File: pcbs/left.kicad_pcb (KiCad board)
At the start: 2 copper layers, 121.1 x 91.2 mm, 27 parts

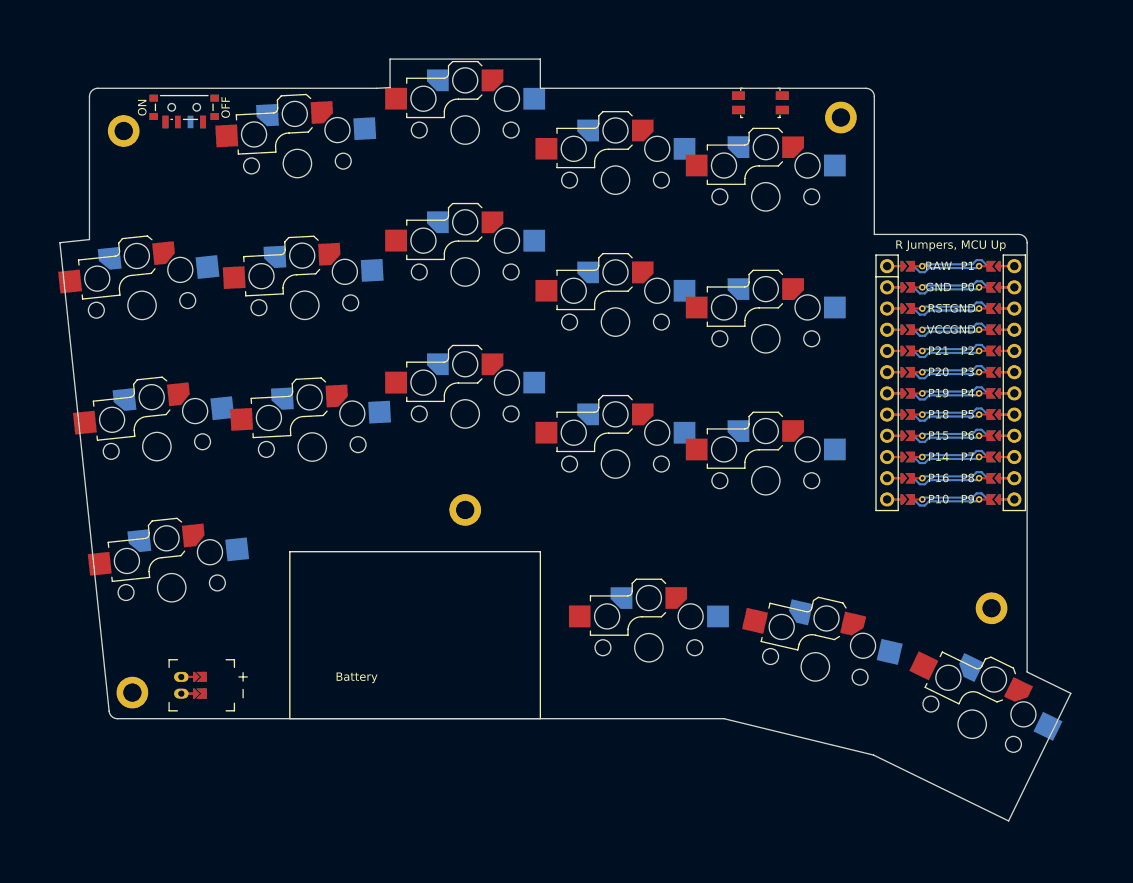
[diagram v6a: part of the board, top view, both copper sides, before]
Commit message: Add 1mm padding to edge
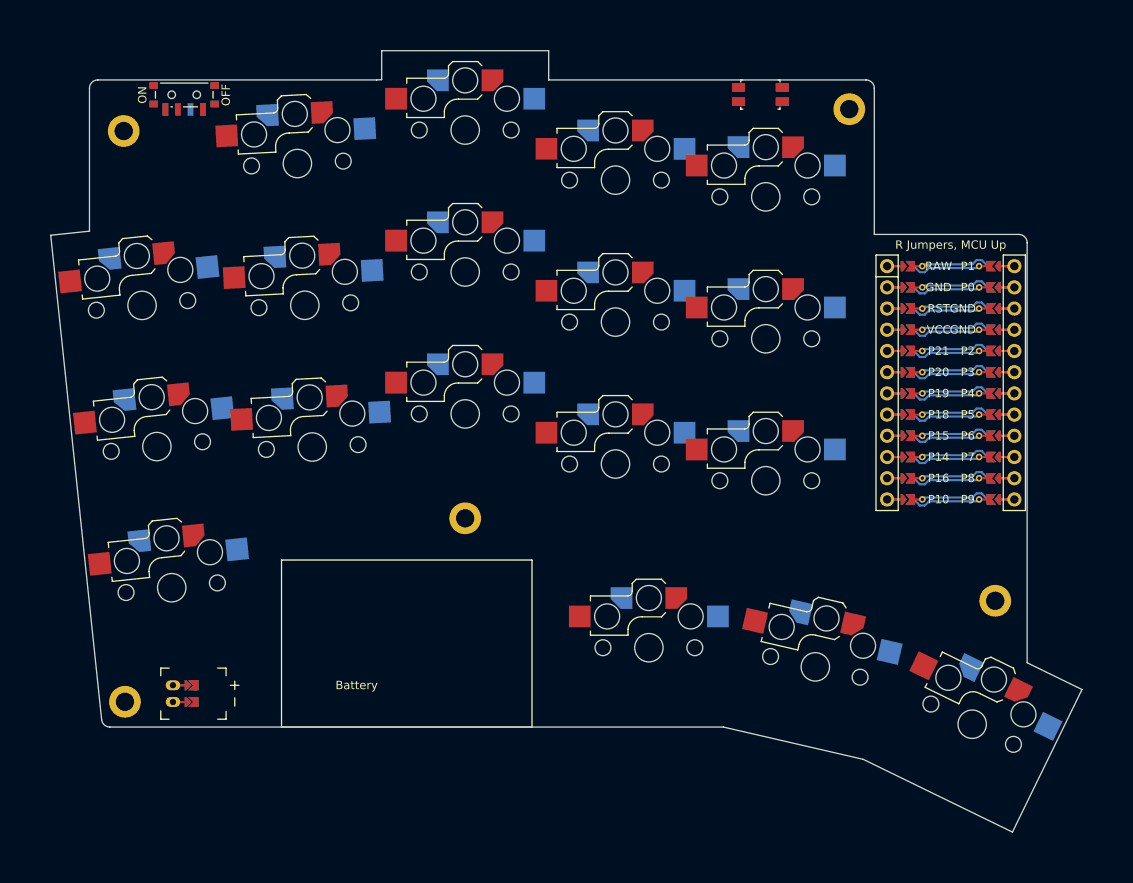
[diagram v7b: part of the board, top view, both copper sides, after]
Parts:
- moved PWR1 1.50 mm to (101.5, 41.0)
- moved H3 1.41 mm to (94.4, 113.7)
- moved H2 1.41 mm to (181.1, 42.7)
- moved JST1 1.41 mm to (100.1, 112.7)
- moved H5 1.00 mm to (198.6, 101.6)
- moved H4 1.00 mm to (135.1, 91.7)
- moved RST1 1.00 mm to (170.5, 40.9)
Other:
- board size 121.1 x 91.2 mm -> 123.5 x 93.6 mm
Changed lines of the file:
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@@
   (footprint "ceoloide:power_switch_smd_side"
     (layer "F.Cu")
-    (at 101.49836669999999 42.48429119999999 90)
+    (at 101.49836669999999 40.98429119999999 90)
     (property "Reference" "PWR1"
       (at -3.6 0 0)
@@
   (footprint "ceoloide:reset_switch_smd_side"
     (layer "F.Cu")
-    (at 170.4983667 41.93429119999999 0)
+    (at 170.4983667 40.93429119999999 0)
     (property "Reference" "RST1"
       (at 0 0 0)
@@
     (footprint "ceoloide:battery_connector_jst_ph_2"
         (layer "F.Cu")
-        (at 101.1483666 111.68429119999999 90)
+        (at 100.1483666 112.68429119999999 90)
         (property "Reference" "JST1"
             (at 0 4.8 90)
@@
         )
     )
-    (segment (start 102.9483666 112.68429119999999) (end 101.1483666 112.68429119999999) (width 0.25) (layer "F.Cu") (net 53))
-    (segment (start 102.9483666 112.68429119999999) (end 101.1483666 112.68429119999999) (width 0.25) (layer "B.Cu") (net 53))
-    (segment (start 102.9483666 110.68429119999999) (end 101.1483666 110.68429119999999) (width 0.25) (layer "F.Cu") (net 54))
-    (segment (start 102.9483666 110.68429119999999) (end 101.1483666 110.68429119999999) (width 0.25) (layer "B.Cu") (net 54))
+    (segment (start 101.9483666 113.68429119999999) (end 100.1483666 113.68429119999999) (width 0.25) (layer "F.Cu") (net 53))
+    (segment (start 101.9483666 113.68429119999999) (end 100.1483666 113.68429119999999) (width 0.25) (layer "B.Cu") (net 53))
+    (segment (start 101.9483666 111.68429119999999) (end 100.1483666 111.68429119999999) (width 0.25) (layer "F.Cu") (net 54))
+    (segment (start 101.9483666 111.68429119999999) (end 100.1483666 111.68429119999999) (width 0.25) (layer "B.Cu") (net 54))
   (gr_text "Battery"
-    (at 122.1483666 110.68429119999999 0)
+    (at 122.1483666 111.68429119999999 0)
     (layer "F.SilkS" )
     (effects
@@
   (footprint "ceoloide:mounting_hole_plated"
     (layer "F.Cu")
-    (at 180.1483666 43.684291099999996 0)
+    (at 181.1483666 42.684291099999996 0)
     (property "Reference" "H2"
       (at 0 3 0)
@@
   (footprint "ceoloide:mounting_hole_plated"
     (layer "F.Cu")
-    (at 95.2872102 112.56143349999999 6)
+    (at 94.3972168 113.6604839 6)
     (property "Reference" "H3"
       (at 0 3 6)
@@
   (footprint "ceoloide:mounting_hole_plated"
     (layer "F.Cu")
-    (at 135.1483667 90.68429119999999 0)
+    (at 135.1483667 91.68429119999999 0)
     (property "Reference" "H4"
       (at 0 3 0)
@@
   (footprint "ceoloide:mounting_hole_plated"
     (layer "F.Cu")
-    (at 198.19092410000002 102.4580398 -26)
+    (at 198.6292952 101.55924569999999 -26)
     (property "Reference" "H5"
       (at 0 3 -26)
@@
     )
   )
-  (gr_line (start 86.60684319999999 58.67357570000001) (end 92.50479308505149 114.78881969999998) (layer Edge.Cuts) (stroke (width 0.15) (type default)))
-(gr_line (start 86.60684319999999 58.67357570000001) (end 90.1483667 58.30134658019551) (layer Edge.Cuts) (stroke (width 0.15) (type default)))
-(gr_line (start 124.57345505196682 40.18429119999999) (end 126.1483667 40.10175357892617) (layer Edge.Cuts) (stroke (width 0.15) (type default)))
-(gr_line (start 144.1483666 40.18429119999999) (end 144.1483667 36.68429119999999) (layer Edge.Cuts) (stroke (width 0.15) (type default)))
-(gr_line (start 144.1483667 36.68429119999999) (end 126.1483667 36.68429119999999) (layer Edge.Cuts) (stroke (width 0.15) (type default)))
-(gr_line (start 126.1483667 36.68429119999999) (end 126.1483667 40.10175357892617) (layer Edge.Cuts) (stroke (width 0.15) (type default)))
-(gr_line (start 93.49931498505148 115.68429119999999) (end 166.1483666 115.68429119999999) (layer Edge.Cuts) (stroke (width 0.15) (type default)))
-(gr_line (start 184.0527886 120.0396531) (end 200.23108150000002 127.93033369999999) (layer Edge.Cuts) (stroke (width 0.15) (type default)))
-(gr_line (start 200.23108150000002 127.93033369999999) (end 207.683391 112.65083489999999) (layer Edge.Cuts) (stroke (width 0.15) (type default)))
-(gr_line (start 207.683391 112.65083489999999) (end 202.4483666 110.09754292235218) (layer Edge.Cuts) (stroke (width 0.15) (type default)))
-(gr_line (start 184.0527886 120.0396531) (end 166.1483666 115.68429119999999) (layer Edge.Cuts) (stroke (width 0.15) (type default)))
+  (gr_line (start 85.50779279999999 57.78358220000001) (end 91.6043889808387 115.78881969999986) (layer Edge.Cuts) (stroke (width 0.15) (type default)))
+(gr_line (start 85.50779279999999 57.78358220000001) (end 90.1483667 57.2958382465655) (layer Edge.Cuts) (stroke (width 0.15) (type default)))
+(gr_line (start 124.54726799407277 39.18429119999999) (end 125.1483667 39.15278895091144) (layer Edge.Cuts) (stroke (width 0.15) (type default)))
+(gr_line (start 145.1483667 39.18429119999999) (end 145.1483667 35.68429119999999) (layer Edge.Cuts) (stroke (width 0.15) (type default)))
+(gr_line (start 145.1483667 35.68429119999999) (end 125.1483667 35.68429119999999) (layer Edge.Cuts) (stroke (width 0.15) (type default)))
+(gr_line (start 125.1483667 35.68429119999999) (end 125.1483667 39.15278895091144) (layer Edge.Cuts) (stroke (width 0.15) (type default)))
+(gr_line (start 92.5989108808387 116.68429119999999) (end 166.06423773916333 116.68429119999999) (layer Edge.Cuts) (stroke (width 0.15) (type default)))
+(gr_line (start 166.06423773916333 116.68429119999999) (end 182.8265398929574 120.55417358778122) (layer Edge.Cuts) (stroke (width 0.15) (type default)))
+(gr_line (start 182.8265398929574 120.55417358778122) (end 200.6915044 129.2674989) (layer Edge.Cuts) (stroke (width 0.15) (type default)))
+(gr_line (start 200.6915044 129.2674989) (end 209.02055620000002 112.190412) (layer Edge.Cuts) (stroke (width 0.15) (type default)))
+(gr_line (start 209.02055620000002 112.190412) (end 202.4483666 108.9849409801272) (layer Edge.Cuts) (stroke (width 0.15) (type default)))
 (gr_line (start 184.1483667 57.684291099999996) (end 201.4483666 57.684291099999996) (layer Edge.Cuts) (stroke (width 0.15) (type default)))
-(gr_line (start 202.4483666 110.09754292235218) (end 202.4483666 58.684291099999996) (layer Edge.Cuts) (stroke (width 0.15) (type default)))
+(gr_line (start 202.4483666 108.9849409801272) (end 202.4483666 58.684291099999996) (layer Edge.Cuts) (stroke (width 0.15) (type default)))
 (gr_arc (start 202.4483666 58.684291099999996) (mid 202.1554734 57.9771843) (end 201.4483666 57.684291099999996) (layer Edge.Cuts) (stroke (width 0.15) (type default)))
-(gr_arc (start 92.50479308505149 114.78881969999996) (mid 92.83018438505148 115.42743599999996) (end 93.49931498505148 115.68429119999996) (layer Edge.Cuts) (stroke (width 0.15) (type default)))
-(gr_line (start 90.1483667 58.30134658019551) (end 90.1483667 41.18429119999999) (layer Edge.Cuts) (stroke (width 0.15) (type default)))
-(gr_line (start 91.1483667 40.18429119999999) (end 124.57345505196682 40.18429119999999) (layer Edge.Cuts) (stroke (width 0.15) (type default)))
-(gr_line (start 144.1483666 40.18429119999999) (end 183.1483667 40.18429119999999) (layer Edge.Cuts) (stroke (width 0.15) (type default)))
-(gr_line (start 184.1483667 41.18429119999999) (end 184.1483667 57.684291099999996) (layer Edge.Cuts) (stroke (width 0.15) (type default)))
-(gr_arc (start 91.1483667 40.18429119999999) (mid 90.44125989999999 40.47718439999999) (end 90.1483667 41.18429119999999) (layer Edge.Cuts) (stroke (width 0.15) (type default)))
-(gr_arc (start 184.1483667 41.18429119999999) (mid 183.8554735 40.47718439999999) (end 183.1483667 40.18429119999999) (layer Edge.Cuts) (stroke (width 0.15) (type default)))
-(gr_line (start 114.1483666 95.68429119999999) (end 114.1483666 115.68429119999999) (layer F.SilkS) (stroke (width 0.15) (type default)))
-(gr_line (start 114.1483666 115.68429119999999) (end 144.1483666 115.68429119999999) (layer F.SilkS) (stroke (width 0.15) (type default)))
-(gr_line (start 144.1483666 115.68429119999999) (end 144.1483666 95.68429119999999) (layer F.SilkS) (stroke (width 0.15) (type default)))
-(gr_line (start 144.1483666 95.68429119999999) (end 114.1483666 95.68429119999999) (layer F.SilkS) (stroke (width 0.15) (type default)))
+(gr_arc (start 91.6043889808387 115.78881969999996) (mid 91.9297802808387 116.42743599999996) (end 92.5989108808387 116.68429119999996) (layer Edge.Cuts) (stroke (width 0.15) (type default)))
+(gr_line (start 90.1483667 57.2958382465655) (end 90.1483667 40.18429119999999) (layer Edge.Cuts) (stroke (width 0.15) (type default)))
+(gr_line (start 91.1483667 39.18429119999999) (end 124.54726799407277 39.18429119999999) (layer Edge.Cuts) (stroke (width 0.15) (type default)))
+(gr_line (start 145.1483667 39.18429119999999) (end 183.1483667 39.18429119999999) (layer Edge.Cuts) (stroke (width 0.15) (type default)))
+(gr_line (start 184.1483667 40.18429119999999) (end 184.1483667 57.684291099999996) (layer Edge.Cuts) (stroke (width 0.15) (type default)))
+(gr_arc (start 91.1483667 39.18429119999999) (mid 90.44125989999999 39.47718439999999) (end 90.1483667 40.18429119999999) (layer Edge.Cuts) (stroke (width 0.15) (type default)))
+(gr_arc (start 184.1483667 40.18429119999999) (mid 183.8554735 39.47718439999999) (end 183.1483667 39.18429119999999) (layer Edge.Cuts) (stroke (width 0.15) (type default)))
+(gr_line (start 113.1483666 96.68429119999999) (end 113.1483666 116.68429119999999) (layer F.SilkS) (stroke (width 0.15) (type default)))
+(gr_line (start 113.1483666 116.68429119999999) (end 143.1483666 116.68429119999999) (layer F.SilkS) (stroke (width 0.15) (type default)))
+(gr_line (start 143.1483666 116.68429119999999) (end 143.1483666 96.68429119999999) (layer F.SilkS) (stroke (width 0.15) (type default)))
+(gr_line (start 143.1483666 96.68429119999999) (end 113.1483666 96.68429119999999) (layer F.SilkS) (stroke (width 0.15) (type default)))
 )
